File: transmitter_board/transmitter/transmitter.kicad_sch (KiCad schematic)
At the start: 9 parts

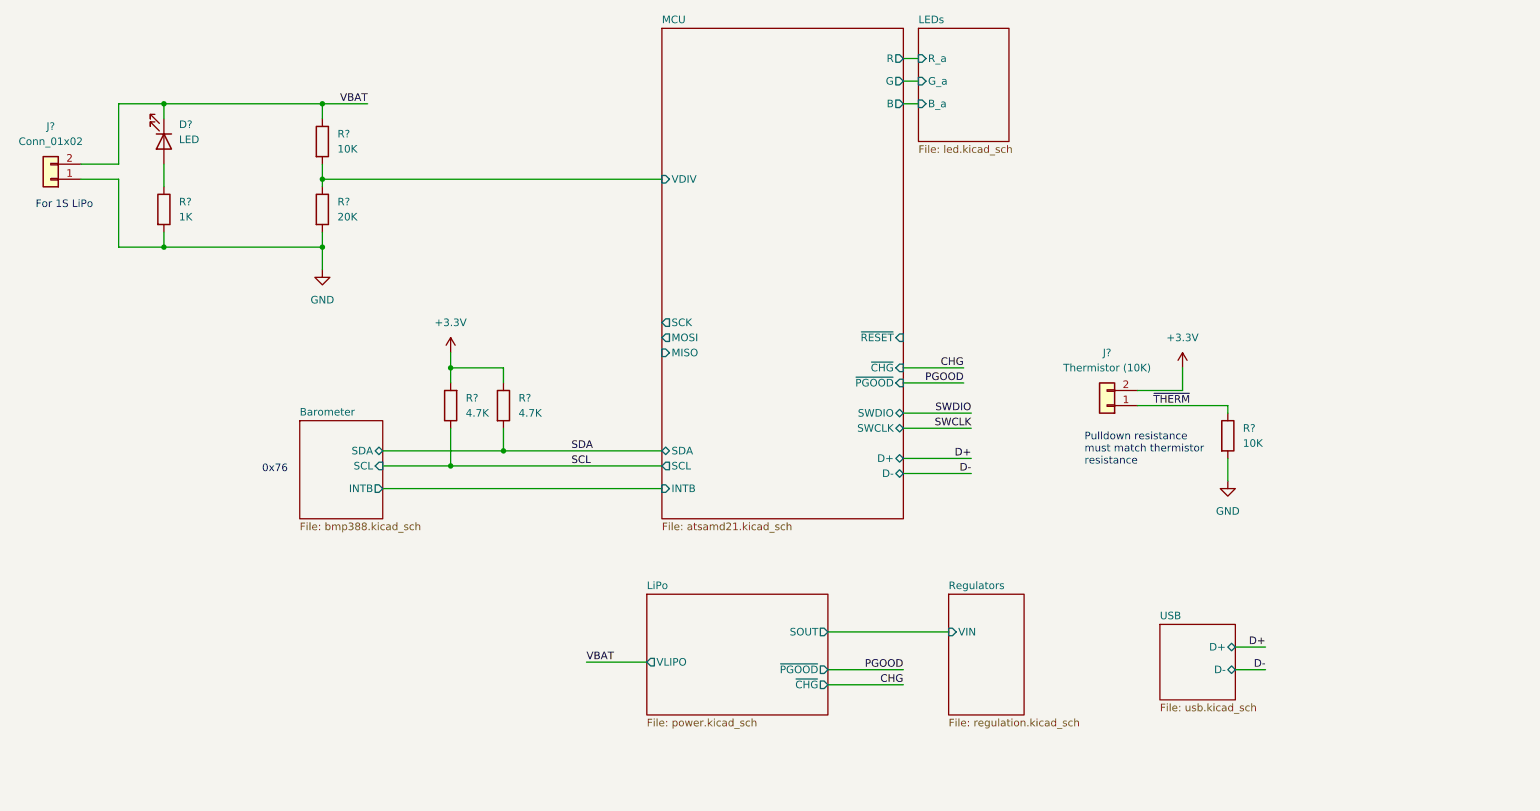
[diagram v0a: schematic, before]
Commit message: finished board schematic
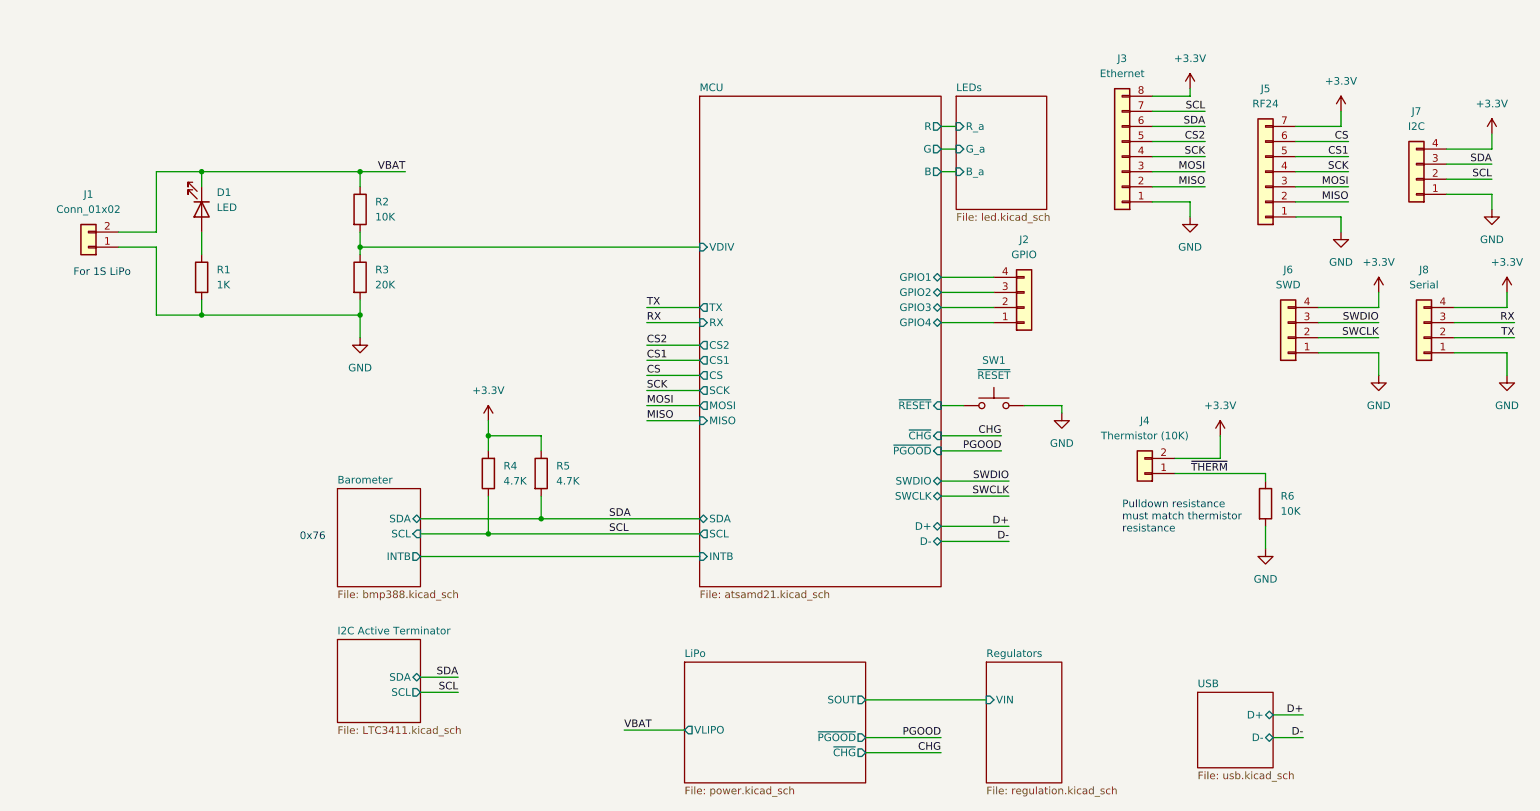
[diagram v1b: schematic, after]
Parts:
- added J2: GPIO, symbol Connector_Generic:Conn_01x04
- added J3: Ethernet, symbol Connector_Generic:Conn_01x08
- added J5: RF24, symbol Connector_Generic:Conn_01x07
- added J6: SWD, symbol Connector_Generic:Conn_01x04
- added J7: I2C, symbol Connector_Generic:Conn_01x04
- added J8: Serial, symbol Connector_Generic:Conn_01x04
- added SW1: ~{RESET}, symbol Switch:SW_Push
- gave numbers to parts that had none: 9
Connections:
- net +3V3: now also J3.8 (Pin_8), J5.7 (Pin_7), J6.4 (Pin_4), J7.4 (Pin_4), J8.4 (Pin_4)
- net GND: now also J3.1 (Pin_1), J5.1 (Pin_1), J6.1 (Pin_1), J7.1 (Pin_1), J8.1 (Pin_1), SW1.2
- net MCU/~{RESET}: now also SW1.1
- net SCL: now also J3.7 (Pin_7), J7.2 (Pin_2)
- net SDA: now also J3.6 (Pin_6), J7.3 (Pin_3)
- net SWCLK: now also J6.2 (Pin_2)
- net SWDIO: now also J6.3 (Pin_3)
- new net CS: J5.6 (Pin_6)
- new net CS1: J5.5 (Pin_5)
- new net CS2: J3.5 (Pin_5)
- new net MCU/GPIO1: J2.4 (Pin_4)
- new net MCU/GPIO2: J2.3 (Pin_3)
- new net MCU/GPIO3: J2.2 (Pin_2)
- new net MCU/GPIO4: J2.1 (Pin_1)
- new net MISO: J3.2 (Pin_2), J5.2 (Pin_2)
- new net MOSI: J3.3 (Pin_3), J5.3 (Pin_3)
- new net RX: J8.3 (Pin_3)
- new net SCK: J3.4 (Pin_4), J5.4 (Pin_4)
- new net TX: J8.2 (Pin_2)
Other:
- added sheet I2C Active Terminator (LTC3411.kicad_sch)
- sheet MCU ports: added CS, CS1, CS2, GPIO1, GPIO2, GPIO3, GPIO4, RX, TX; removed none
- moved on the sheet: D1, J1, J4, R1, R2, R3, R4, R5, R6
